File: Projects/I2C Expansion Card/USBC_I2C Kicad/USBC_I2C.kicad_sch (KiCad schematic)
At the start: 13 parts, among them U1 MCP2221A

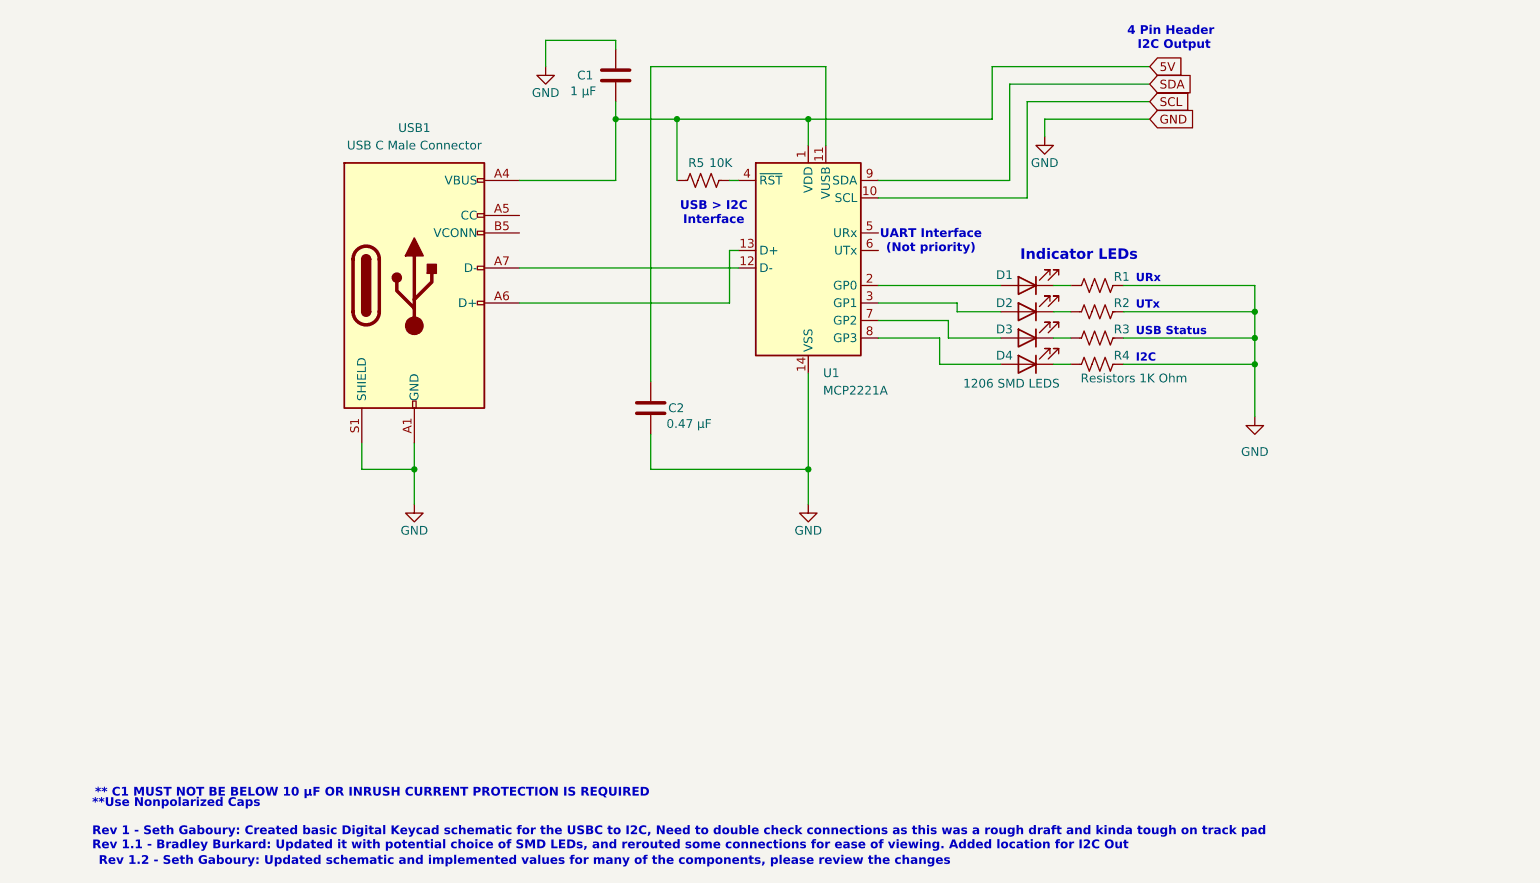
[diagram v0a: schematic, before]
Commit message: Swapped to SMD chip
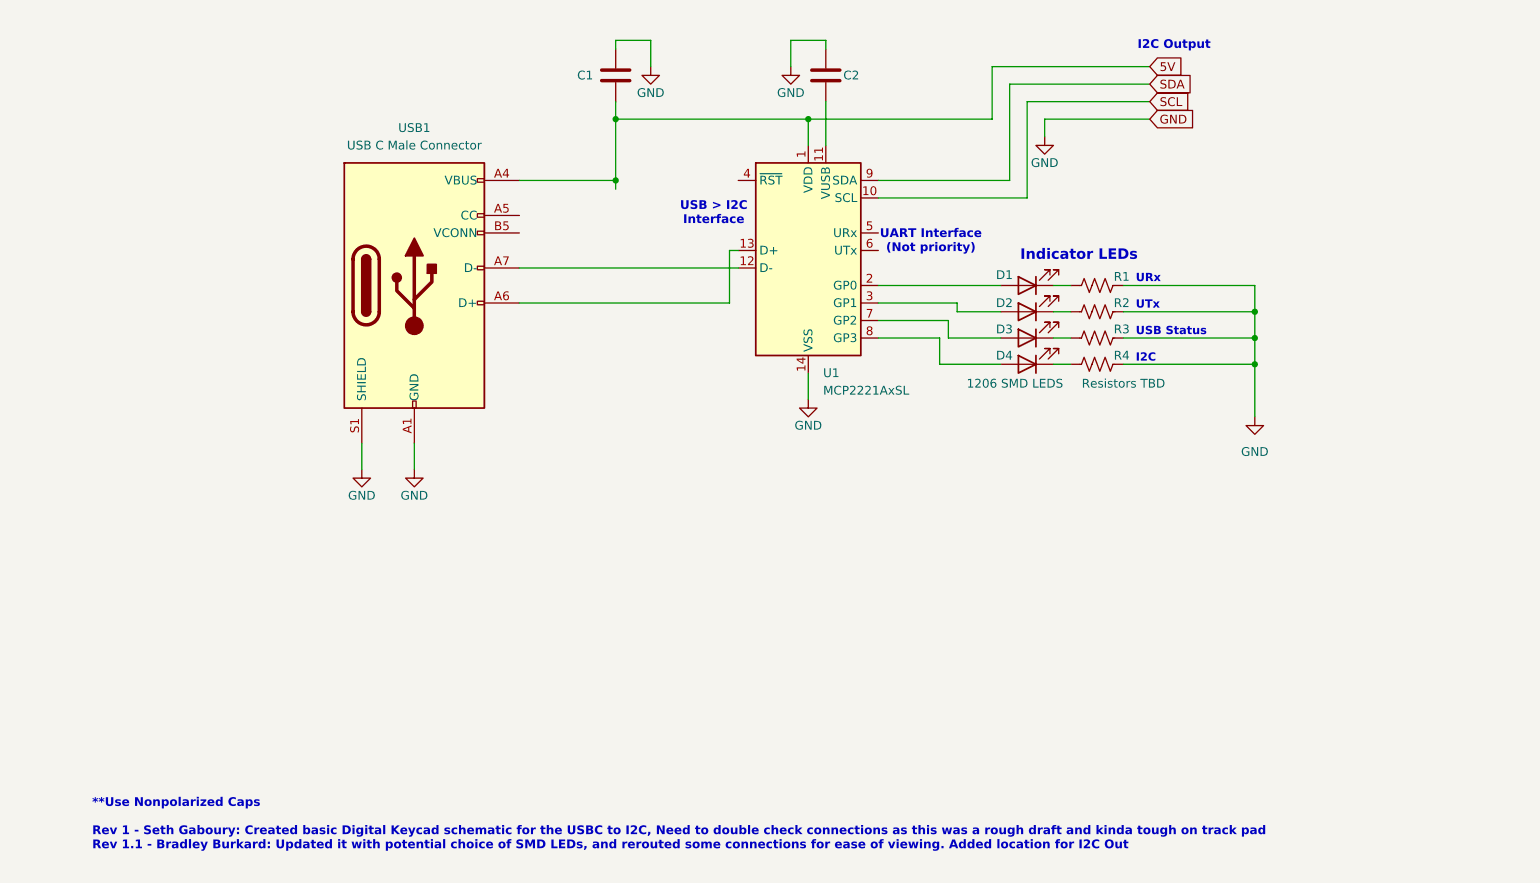
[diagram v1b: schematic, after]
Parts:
- removed R5: 10K, symbol Device:R_US
- removed U1: MCP2221A, Package_DIP:DIP-14_W7.62mm, symbol Interface_USB:MCP2221AxP
- added U1: MCP2221AxSL, Package_SO:SOIC-14_3.9x8.7mm_P1.27mm, symbol Interface_USB:MCP2221AxSL
- C1: value 1 μF -> C; footprint (none) -> C_0603_1608Metric
- C2: value 0.47 μF -> C; footprint (none) -> C_0603_1608Metric
- R1: value Resistors 1K Ohm -> Resistors TBD
- USB1: footprint (none) -> USB_C_Plug_Molex_105444
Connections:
- net 5V: now also U1.1 (VDD)
- net GND: now also C2.1, U1.14 (VSS); no longer C2.2
- net SCL: now also U1.10 (SCL)
- net SDA: now also U1.9 (SDA)
- net at USB1.A6 (D+): now also U1.13 (D+)
- net at USB1.A7 (D-): now also U1.12 (D-)
- net at D2.2 (A): now also U1.3 (GP1)
- net at D3.2 (A): now also U1.7 (GP2)
- net at D1.2 (A): now also U1.2 (GP0)
- net at D4.2 (A): now also U1.8 (GP3)
- new net: C2.2, U1.11 (VUSB)
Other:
- note removed: "** C1 MUST NOT BE BELOW 10 μF OR INRUSH CURRENT PROTECTION IS REQUIRED"
- note removed: "4 Pin Header"
- note removed: "Rev 1.2 - Seth Gaboury: Updated schematic and implemented values for many of the components, please review the changes"
- moved on the sheet: C2

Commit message: Added capacitor values
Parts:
- C1: value C -> 0.47uF
- C2: value C -> 0.22uF
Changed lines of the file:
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@@
 			)
 		)
-		(property "Value" "C"
+		(property "Value" "0.47uF"
 			(at 83.312 34.036 0)
 			(effects
@@
 			)
 		)
-		(property "Value" "C"
+		(property "Value" "0.22uF"
 			(at 123.19 34.2899 0)
 			(effects

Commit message: Reworked pcb to put everything on one board
Merged the 3 versions into one, added through hole cap holes, added uart switch, fixed the pcb edge
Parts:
- C1, C2: footprint C_0603_1608Metric -> C_1206_3216Metric_Pad1.33x1.80mm_HandSolder
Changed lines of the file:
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@@
 			)
 		)
-		(property "Footprint" "C_0603_1608Metric"
+		(property "Footprint" "C_1206_3216Metric_Pad1.33x1.80mm_HandSolder"
 			(at 89.8652 36.83 0)
 			(effects
@@
 			)
 		)
-		(property "Footprint" "C_0603_1608Metric"
+		(property "Footprint" "C_1206_3216Metric_Pad1.33x1.80mm_HandSolder"
 			(at 120.3452 36.83 0)
 			(effects

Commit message: Fixing some DRC
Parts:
- added SW1: SW_DIP_x04, SW_DIP_SPSTx04_Slide_Copal_CHS-04B_W7.62mm_P1.27mm, symbol Switch:SW_DIP_x04
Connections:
- net at U1.5 (URx): now also SW1.3
- net at U1.6 (UTx): now also SW1.4
- net SCL: no longer names the net of U1.10 (SCL)
- net SCL: now also SW1.2
- net SDA: no longer names the net of U1.9 (SDA)
- net SDA: now also SW1.1
- new net Out0: SW1.6, SW1.8
- new net Out1: SW1.5, SW1.7
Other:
- note added: "Output"
- note removed: "I2C Output"
- note removed: "UART Interface (Not priority)"

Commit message: Added USB PD Resistors
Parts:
- added R1: 5.1k, R_1206_3216Metric, symbol Device:R_US
- added R2: Resistors TBD, R_1206_3216Metric, symbol Device:R_US
- renumbered R1 to R5, R2 to R6
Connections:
- net GND: now also R1.2, R2.2
- net at USB1.A5 (CC): now also R1.1
- net at USB1.B5 (VCONN): now also R2.1

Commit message: Added OCP
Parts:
- added F1: Polyfuse, Fuse_1206_3216Metric, symbol Device:Polyfuse
- added F2: Polyfuse, symbol Device:Polyfuse
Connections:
- net 5V: no longer names the net of C1.2, U1.1 (VDD), USB1.A4 (VBUS), USB1.A9 (VBUS), USB1.B4 (VBUS), USB1.B9 (VBUS)
- net 5V: now also F1.1
- new net Vo: F1.2

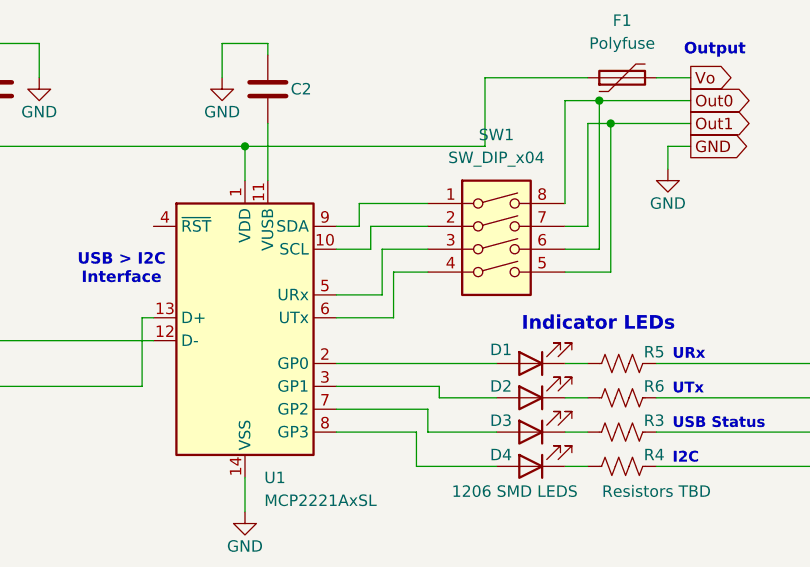
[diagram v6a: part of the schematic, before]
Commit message: Reworked the PCB to better route traces
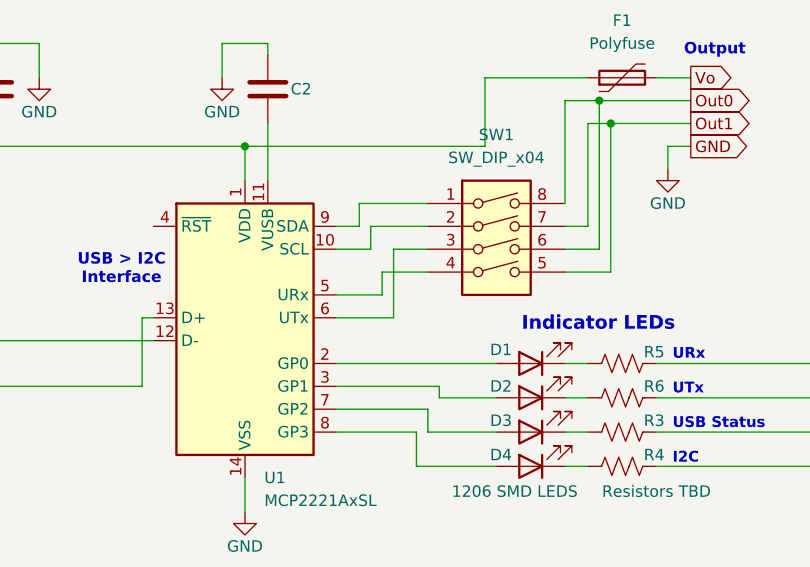
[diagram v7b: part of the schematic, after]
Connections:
- net at SW1.3: now also U1.6 (UTx); no longer U1.5 (URx)
- net at SW1.4: now also U1.5 (URx); no longer U1.6 (UTx)
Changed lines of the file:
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@@
+	(wire
+		(pts
+			(xy 132.08 53.34) (xy 137.16 53.34)
+		)
+		(stroke
+			(width 0)
+			(type default)
+		)
+	)
 	(wire
 		(pts
@@
 	(wire
 		(pts
-			(xy 132.08 50.8) (xy 137.16 50.8)
-		)
-		(stroke
-			(width 0)
-			(type default)
-		)
-	)
-	(wire
-		(pts
 			(xy 162.56 31.75) (xy 166.37 31.75)
 		)
@@
 	(wire
 		(pts
+			(xy 133.35 50.8) (xy 137.16 50.8)
+		)
+		(stroke
+			(width 0)
+			(type default)
+		)
+	)
+	(wire
+		(pts
 			(xy 181.61 74.93) (xy 181.61 82.55)
 		)
@@
 	(wire
 		(pts
-			(xy 132.08 55.88) (xy 132.08 50.8)
-		)
-		(stroke
-			(width 0)
-			(type default)
-		)
-	)
-	(wire
-		(pts
 			(xy 74.93 66.04) (xy 105.41 66.04)
 		)
@@
 	(wire
 		(pts
+			(xy 132.08 55.88) (xy 132.08 53.34)
+		)
+		(stroke
+			(width 0)
+			(type default)
+		)
+	)
+	(wire
+		(pts
 			(xy 162.56 67.31) (xy 181.61 67.31)
 		)
@@
 	(wire
 		(pts
-			(xy 133.35 53.34) (xy 133.35 58.42)
+			(xy 133.35 50.8) (xy 133.35 58.42)
 		)
 		(stroke
@@
 		)
 		(stroke
-			(width 0)
-			(type default)
-		)
-	)
-	(wire
-		(pts
-			(xy 137.16 53.34) (xy 133.35 53.34)
-		)
-		(stroke

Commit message: Swapped switches
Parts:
- SW1: footprint SW_DIP_SPSTx04_Slide_Copal_CHS-04B_W7.62mm_P1.27mm -> SW_DIP_SPSTx04_Slide_Omron_A6H-4101_W6.15mm_P1.27mm
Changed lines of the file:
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@@
 			)
 		)
-		(property "Footprint" "SW_DIP_SPSTx04_Slide_Copal_CHS-04B_W7.62mm_P1.27mm"
+		(property "Footprint" "SW_DIP_SPSTx04_Slide_Omron_A6H-4101_W6.15mm_P1.27mm"
 			(at 144.78 50.8 0)
 			(effects
